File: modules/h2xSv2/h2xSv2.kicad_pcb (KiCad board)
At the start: 2 copper layers, 95.2 x 40.6 mm, 19 parts, among them J1 Conn_01x10_Male, J10 Conn_01x02_Male, J11 Conn_01x06_Male, J2 Conn_01x10_Male, J3 Conn_01x10_Male, J4 Conn_01x10_Male, J5 Conn_01x04_Male, J6 Conn_01x04_Male, J7 Conn_01x12_Male, J8 Conn_01x12_Male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

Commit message: Fix sizes
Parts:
- moved J11 1.27 mm to (66.0, 22.9)
- moved H1 1.27 mm to (58.4, 58.4)
- moved H3 1.27 mm to (58.4, 25.4)
- moved J10 1.27 mm to (58.4, 34.9)
- moved H2 1.27 mm to (91.4, 58.4)
- moved H4 1.27 mm to (91.4, 25.4)
- moved J1 1.27 mm to (86.4, 25.4)
- moved J2 1.27 mm to (86.4, 58.4)
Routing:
- net VCC: track 136.5 -> 135.2 mm
- net GND: track 168.3 -> 167.0 mm
- net /A5: track 106.8 -> 105.5 mm
- net /A4: track 108.7 -> 107.5 mm
- net /A3: track 65.9 -> 64.6 mm
- net /5: track 92.8 -> 91.5 mm
- net /3: track 102.6 -> 101.3 mm
- net /13: track 75.1 -> 73.8 mm
- net /12: track 70.5 -> 69.3 mm
- net /11: track 66.1 -> 64.8 mm
- net /A2: track 64.0 -> 62.7 mm
- net /A0: track 60.2 -> 58.9 mm
- net /9: track 75.1 -> 73.9 mm
- net /8: track 79.7 -> 78.5 mm
- net /7: track 84.0 -> 82.7 mm
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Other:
- board size 95.2 x 40.6 mm -> 94 x 40.6 mm

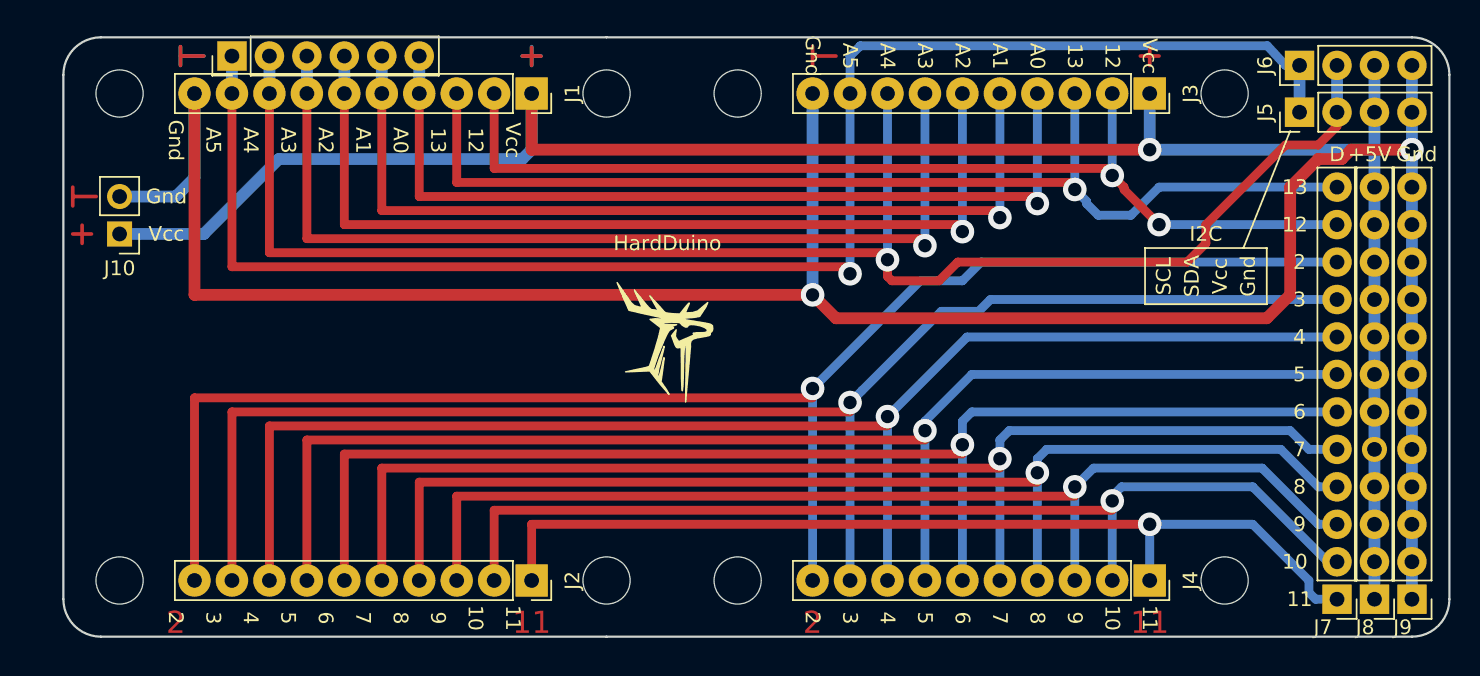
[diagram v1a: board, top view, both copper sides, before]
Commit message: h2xSv2 - Fix grid to 2.54 & mounting holes
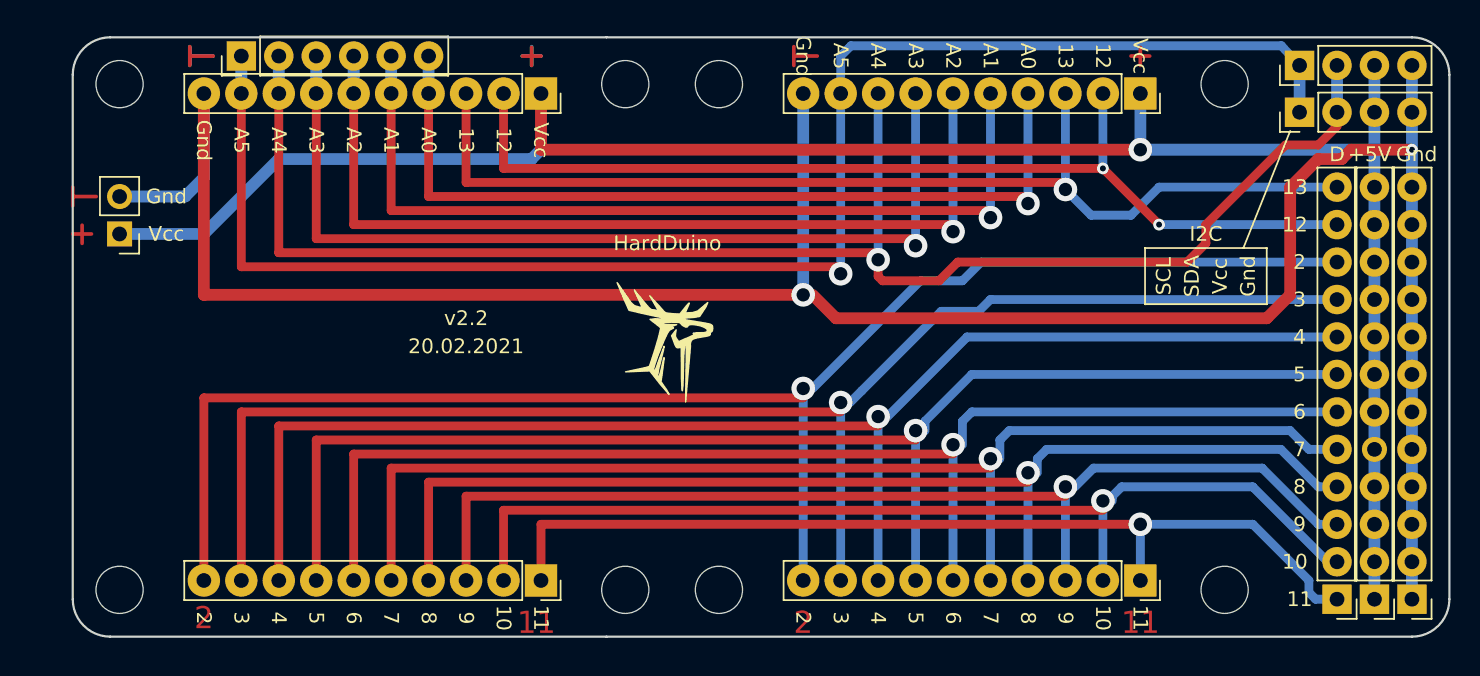
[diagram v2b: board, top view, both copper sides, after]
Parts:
- moved H2 1.42 mm to (92.7, 59.1)
- moved H4 1.42 mm to (92.7, 24.8)
- moved H6 1.42 mm to (99.1, 24.8)
- moved H8 1.42 mm to (99.1, 59.1)
- moved J1 0.64 mm to (87.0, 25.4)
- moved J2 0.64 mm to (87.0, 58.4)
- moved J3 0.64 mm to (127.6, 25.4)
- moved J4 0.64 mm to (127.6, 58.4)
- moved H1 0.63 mm to (58.4, 59.1)
- moved H3 0.63 mm to (58.4, 24.8)
- moved H5 0.63 mm to (133.3, 24.8)
- moved H7 0.63 mm to (133.3, 59.1)
- moved J11 0.63 mm to (66.7, 22.9)
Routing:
- net /A0: track 58.9 -> 57.6 mm
- net /8: track 78.5 -> 77.2 mm
- net /5: track 91.5 -> 90.2 mm
- net /4: track 96.2 -> 94.9 mm
- net /10: track 70.0 -> 68.7 mm
- net /11: track 64.8 -> 63.5 mm
- net /A3: track 64.6 -> 63.3 mm
- net /A2: track 62.7 -> 61.4 mm
- net /A1: track 60.8 -> 59.5 mm
- net /9: track 73.9 -> 72.6 mm
- net /7: track 82.7 -> 81.4 mm
- net /6: track 86.9 -> 85.7 mm
- net /3: track 101.3 -> 100.0 mm
- net /2: track 106.4 -> 105.2 mm
- net /12: track 69.3 -> 68.3 mm
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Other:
- board size 94 x 40.6 mm -> 93.3 x 40.6 mm
- board text added: "20.02.2021"
- board text added: "v2.2"

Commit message: Now 2x shields have distance between 1x parts
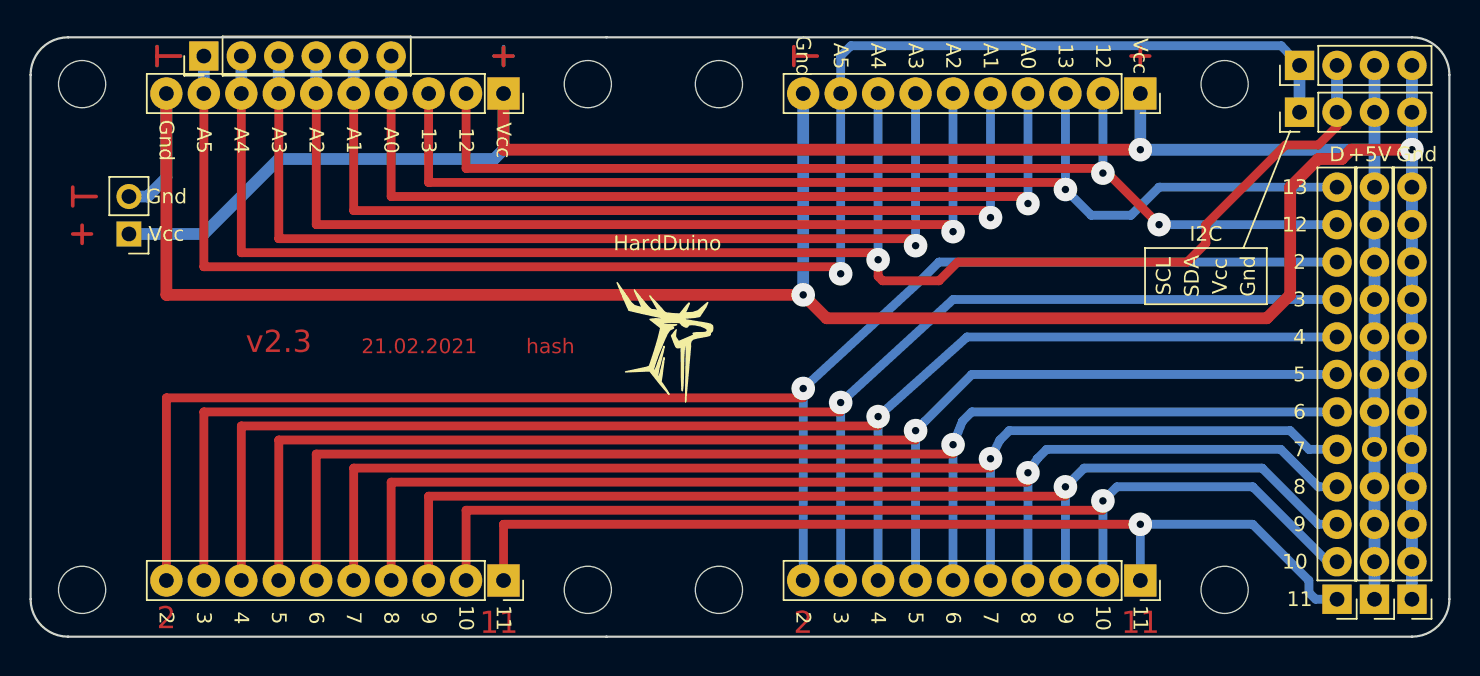
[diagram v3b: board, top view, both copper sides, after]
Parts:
- moved J1 2.54 mm to (84.5, 25.4)
- moved J2 2.54 mm to (84.5, 58.4)
- moved H1 2.54 mm to (55.9, 59.1)
- moved H3 2.54 mm to (55.9, 24.8)
- moved H2 2.54 mm to (90.2, 59.1)
- moved H4 2.54 mm to (90.2, 24.8)
- moved J11 2.54 mm to (64.1, 22.9)
- moved J10 0.63 mm to (59.1, 34.9)
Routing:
- net /11: track 63.5 -> 66.7 mm
- net /9: track 72.6 -> 75.8 mm
- net /4: track 94.9 -> 97.9 mm
- net /3: track 100.0 -> 103.0 mm
- net /2: track 105.2 -> 108.1 mm
- net /10: track 68.7 -> 71.7 mm
- net /5: track 90.2 -> 93.0 mm
- net /8: track 77.2 -> 79.9 mm
- net /7: track 81.4 -> 84.1 mm
- net /6: track 85.7 -> 88.3 mm
- net /A2: track 61.4 -> 64.0 mm
- net /A0: track 57.6 -> 60.2 mm
- net /13: track 73.1 -> 75.6 mm
- net /A5: track 104.9 -> 107.4 mm
- net /A4: track 106.8 -> 109.4 mm
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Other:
- board size 93.3 x 40.6 mm -> 96.2 x 40.6 mm
- board text added: "21.02.2021"
- board text added: "hash"
- board text added: "v2.3"
- board text removed: "20.02.2021"
- board text removed: "v2.2"

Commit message: Fix left Edge.Cuts
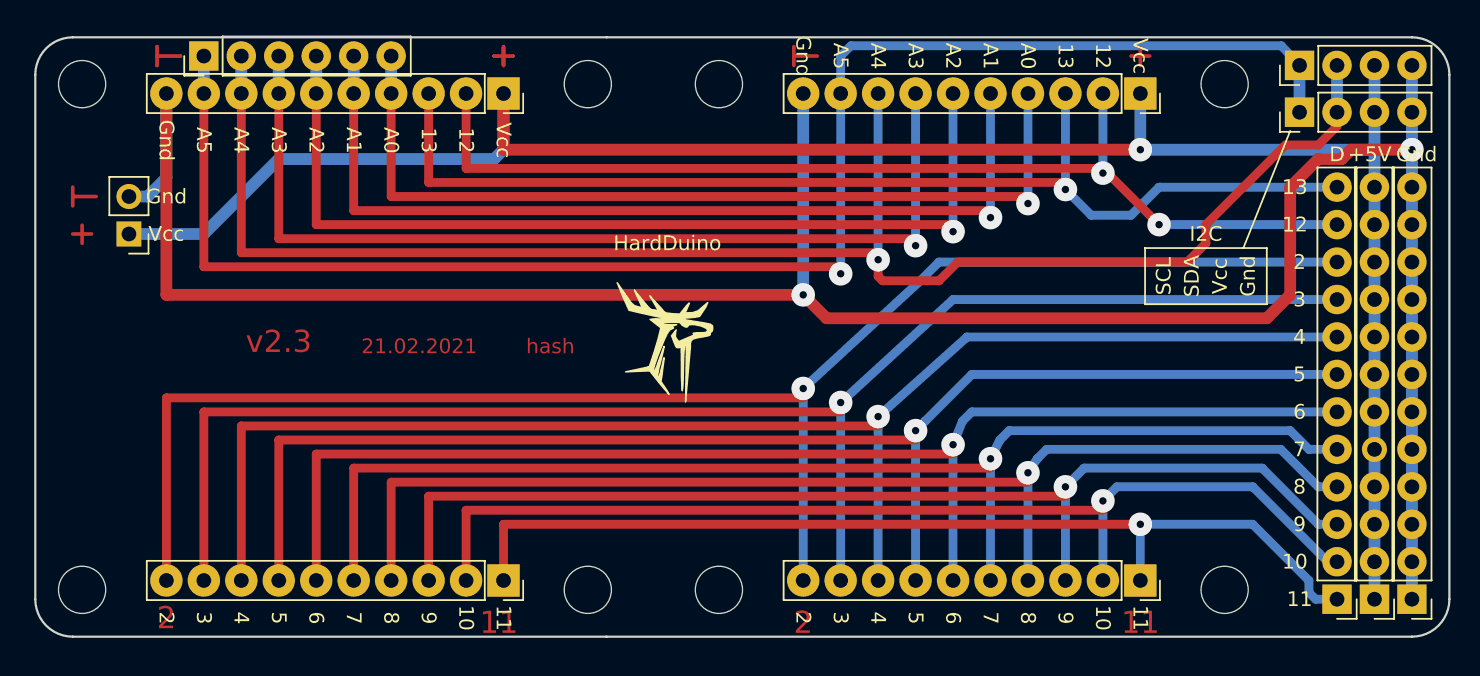
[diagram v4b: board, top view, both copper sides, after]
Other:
- board size 96.2 x 40.6 mm -> 95.9 x 40.6 mm

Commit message: Move mounting holes closer
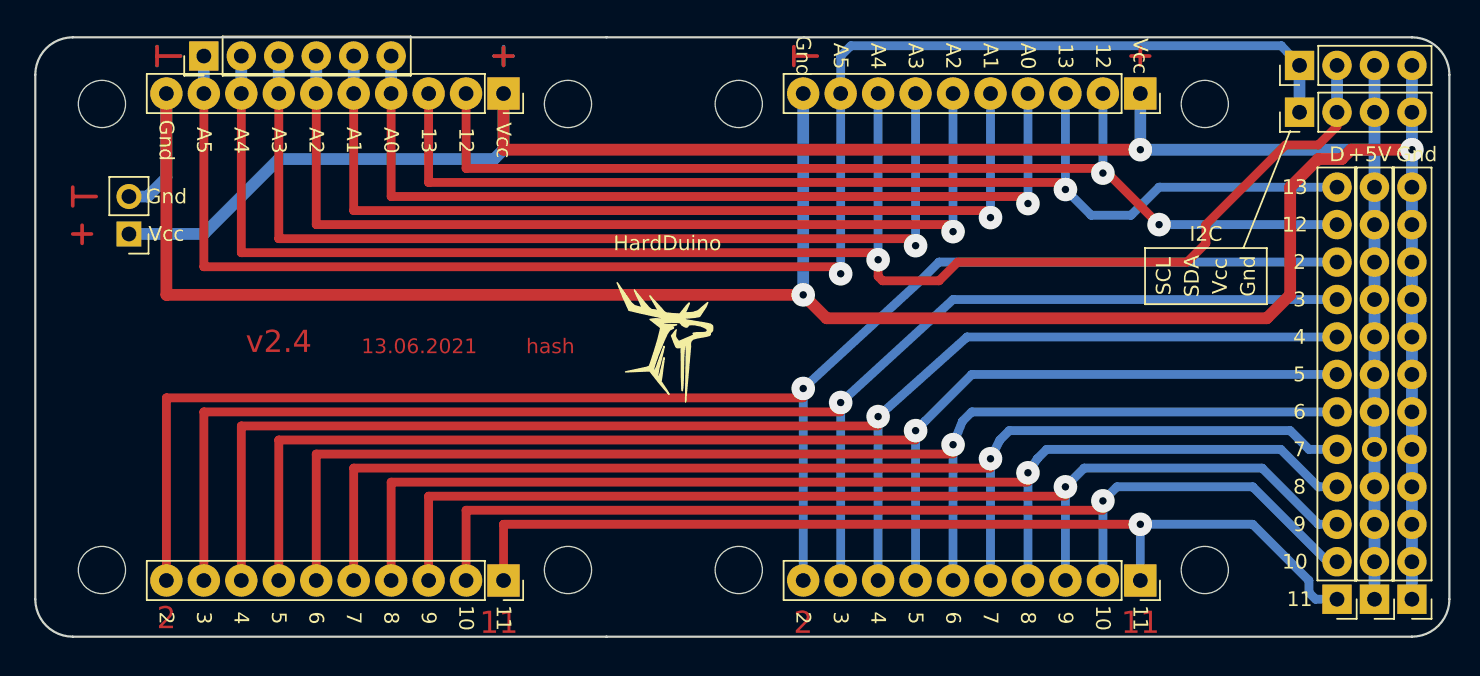
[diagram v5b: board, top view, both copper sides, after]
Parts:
- moved H1 1.90 mm to (57.2, 57.7)
- moved H2 1.90 mm to (88.8, 57.7)
- moved H3 1.90 mm to (57.2, 26.1)
- moved H4 1.90 mm to (88.8, 26.1)
- moved H5 1.90 mm to (132.0, 26.1)
- moved H6 1.90 mm to (100.4, 26.1)
- moved H7 1.90 mm to (132.0, 57.7)
- moved H8 1.90 mm to (100.4, 57.7)
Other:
- board text added: "13.06.2021"
- board text added: "v2.4"
- board text removed: "21.02.2021"
- board text removed: "v2.3"
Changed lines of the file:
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@@
   )
   (module MountingHole:MountingHole_3.2mm_M3 (layer F.Cu)
-    (at 55.88 59.055 90)
+    (at 57.225 57.71 90)
     (descr "Mounting Hole 3.2mm, no annular, M3")
     (tags "mounting hole 3.2mm no annular m3")
@@
   )
   (module MountingHole:MountingHole_3.2mm_M3 (layer F.Cu)
-    (at 90.17 59.055 90)
+    (at 88.825 57.71 90)
     (descr "Mounting Hole 3.2mm, no annular, M3")
     (tags "mounting hole 3.2mm no annular m3")
@@
   )
   (module MountingHole:MountingHole_3.2mm_M3 (layer F.Cu)
-    (at 55.88 24.765 90)
+    (at 57.225 26.11 90)
     (descr "Mounting Hole 3.2mm, no annular, M3")
     (tags "mounting hole 3.2mm no annular m3")
@@
   )
   (module MountingHole:MountingHole_3.2mm_M3 (layer F.Cu)
-    (at 90.17 24.765 90)
+    (at 88.825 26.11 90)
     (descr "Mounting Hole 3.2mm, no annular, M3")
     (tags "mounting hole 3.2mm no annular m3")
@@
   )
   (module MountingHole:MountingHole_3.2mm_M3 (layer F.Cu)
-    (at 133.35 24.765)
+    (at 132.005 26.11)
     (descr "Mounting Hole 3.2mm, no annular, M3")
     (tags "mounting hole 3.2mm no annular m3")
@@
   )
   (module MountingHole:MountingHole_3.2mm_M3 (layer F.Cu)
-    (at 99.06 24.765)
+    (at 100.405 26.11)
     (descr "Mounting Hole 3.2mm, no annular, M3")
     (tags "mounting hole 3.2mm no annular m3")
@@
   )
   (module MountingHole:MountingHole_3.2mm_M3 (layer F.Cu)
-    (at 133.35 59.055)
+    (at 132.005 57.71)
     (descr "Mounting Hole 3.2mm, no annular, M3")
     (tags "mounting hole 3.2mm no annular m3")
@@
   )
   (module MountingHole:MountingHole_3.2mm_M3 (layer F.Cu)
-    (at 99.06 59.055)
+    (at 100.405 57.71)
     (descr "Mounting Hole 3.2mm, no annular, M3")
     (tags "mounting hole 3.2mm no annular m3")
@@
     (effects (font (size 1 1) (thickness 0.2)))
   )
-  (gr_text 21.02.2021 (at 78.74 42.545) (layer F.Cu)
+  (gr_text 13.06.2021 (at 78.74 42.545) (layer F.Cu)
     (effects (font (size 1 1) (thickness 0.2)))
   )
-  (gr_text v2.3 (at 69.215 42.2275) (layer F.Cu)
+  (gr_text v2.4 (at 69.215 42.2275) (layer F.Cu)
     (effects (font (size 1.5 1.5) (thickness 0.3)))
   )

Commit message: h2xSv2 - now v2.5
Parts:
- moved J6 1.90 mm to (138.4, 25.4)
- moved J5 1.27 mm to (138.4, 27.9)
- moved J7 1.27 mm to (141.0, 58.4)
- moved J8 1.27 mm to (143.5, 58.4)
- moved J9 1.27 mm to (146.1, 58.4)
- moved H1 0.30 mm to (57.1, 57.5)
- moved H3 0.30 mm to (57.1, 26.4)
- moved H2 0.30 mm to (89.0, 57.5)
- moved H4 0.30 mm to (89.0, 26.4)
- moved H5 0.30 mm to (132.2, 26.4)
- moved H6 0.30 mm to (100.2, 26.4)
- moved H7 0.30 mm to (132.2, 57.5)
- moved H8 0.30 mm to (100.2, 57.5)
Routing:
- net GND: track 166.4 -> 175.6 mm, vias 2 -> 1
- net /A4: track 109.4 -> 116.2 mm
- net VCC: track 133.9 -> 137.5 mm
- net /A5: track 107.4 -> 108.7 mm
- net /11: track 66.7 -> 65.7 mm
- net /8: track 79.9 -> 79.4 mm
- net /9: track 75.8 -> 75.2 mm
- net /7: track 84.1 -> 83.6 mm
- net /6: track 88.3 -> 88.9 mm
- net /5: track 93.0 -> 93.5 mm
- net /3: track 103.0 -> 103.6 mm
- net /2: track 108.1 -> 108.7 mm
- net /13: track 75.6 -> 76.2 mm
- net /12: track 70.8 -> 71.3 mm
- net /10: track 71.7 -> 71.2 mm
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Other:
- board text added: "22.06.2021"
- board text added: "v2.5"
- board text removed: "13.06.2021"
- board text removed: "v2.4"

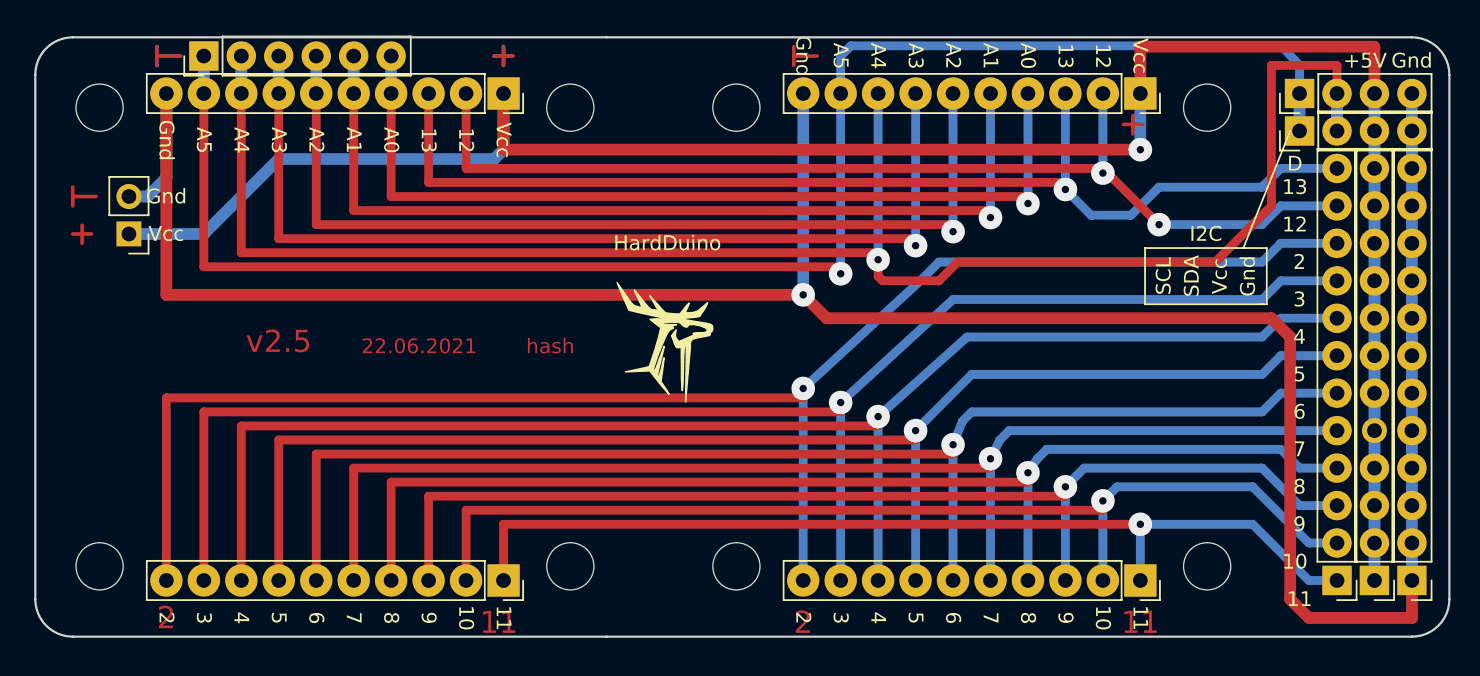
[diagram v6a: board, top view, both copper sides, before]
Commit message: Fix routes on h2xS
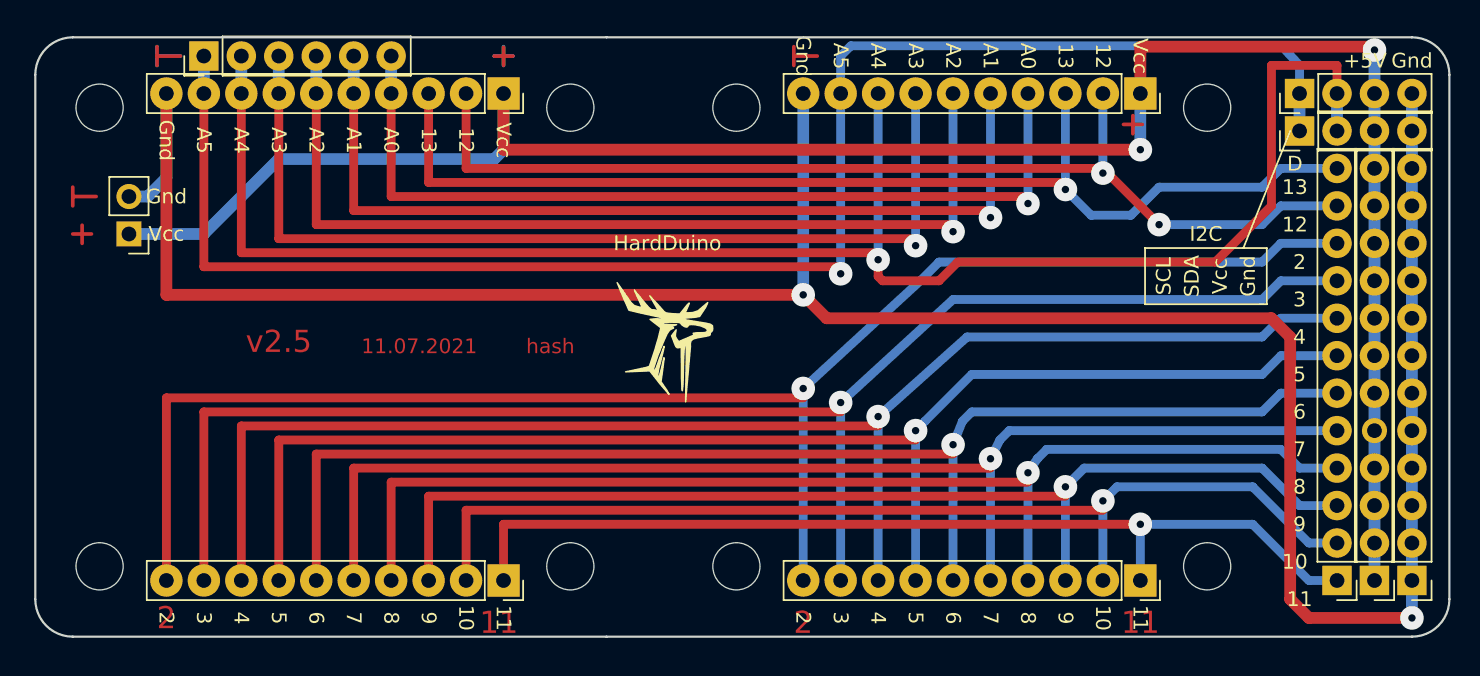
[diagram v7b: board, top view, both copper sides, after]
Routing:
- net GND: vias 1 -> 2
- net VCC: vias 1 -> 2
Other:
- board text added: "11.07.2021"
- board text removed: "22.06.2021"

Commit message: New hash on h2xS
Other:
- board text added: "c90e5e"
- board text removed: "hash"
